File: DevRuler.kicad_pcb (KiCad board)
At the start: 2 copper layers, 205 x 30 mm, 2 parts

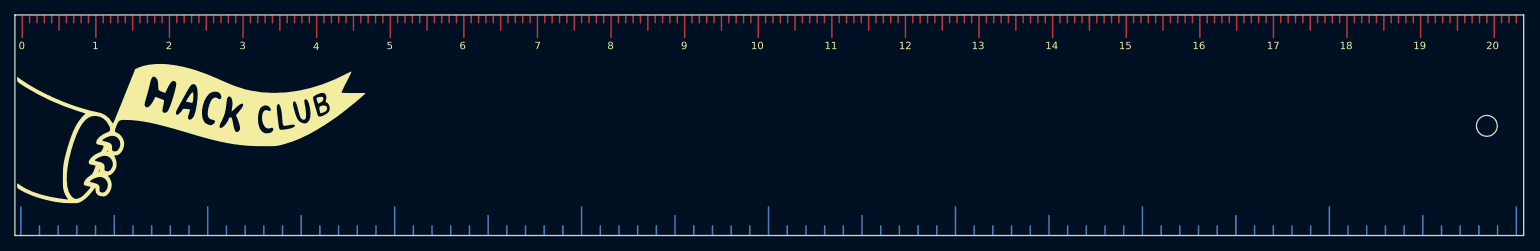
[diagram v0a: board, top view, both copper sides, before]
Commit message: Update LOGO footprint UUIDs, position and silkscreen
Modify DevRuler.kicad_pcb LOGO footprint: replace multiple UUIDs, change the footprint origin (from at 230 93 180 to at 152.5 97), and move/rewrap silkscreen polygons from B.SilkS to F.SilkS with updated fp_poly coordinates. These edits reposition and refresh the logo artwork on the front silkscreen and update element identifiers; no pad/net definitions were altered.
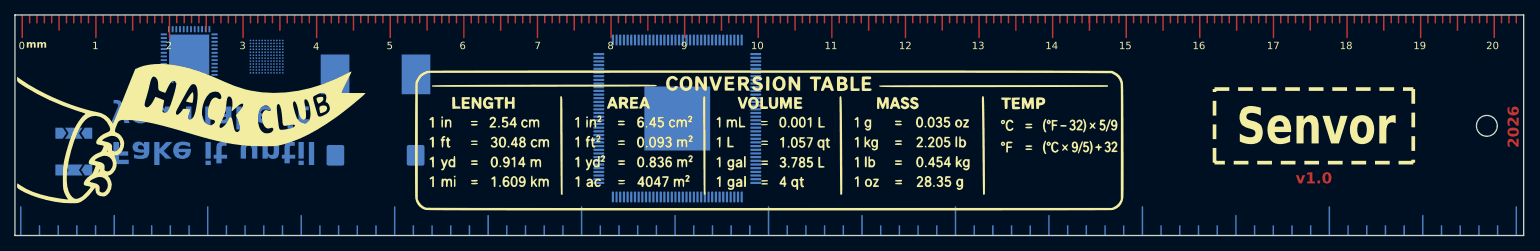
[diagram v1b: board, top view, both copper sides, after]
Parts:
- added G***: LOGO, LOGO, F.Cu at (152.5, 97.0)
- added G***: LOGO, LOGO, B.Cu at (187.0, 93.0)
- added REF**: ST_WLCSP-144_Die470, Package_CSP:ST_WLCSP-144_Die470, B.Cu at (84.2, 85.6)
- added REF**: EQFP-144-1EP_20x20mm_P0.5mm_EP8.93x8.7mm, Package_QFP:EQFP-144-1EP_20x20mm_P0.5mm_EP8.93x8.7mm, B.Cu at (140.0, 94.0)
- added REF**: OSHW-Symbol_13.4x12mm_SilkScreen, Symbol:OSHW-Symbol_13.4x12mm_SilkScreen, B.Cu at (58.0, 87.0)
- added REF**: SolderJumper-3_P2.0mm_Open_TrianglePad1.0x1.5mm, Jumper:SolderJumper-3_P2.0mm_Open_TrianglePad1.0x1.5mm, B.Cu at (58.0, 96.0)
- added REF**: L_Neosid_SM-NE127_HandSoldering, Inductor_SMD:L_Neosid_SM-NE127_HandSoldering, B.Cu at (99.0, 88.0)
- added REF**: Jumper_Harwin_S1621_P10.9mm, Jumper:Jumper_Harwin_S1621_P10.9mm, B.Cu at (99.0, 99.0)
- added REF**: Polarity_Center_Negative_6mm_SilkScreen, Symbol:Polarity_Center_Negative_6mm_SilkScreen, B.Cu at (117.0, 94.0)
- added REF**: QFN-48-1EP_7x7mm_P0.5mm_EP5.45x5.45mm, Package_DFN_QFN:QFN-48-1EP_7x7mm_P0.5mm_EP5.45x5.45mm, B.Cu at (73.7, 85.3)
- added REF**: SolderJumper-3_P2.0mm_Open_TrianglePad1.0x1.5mm, Jumper:SolderJumper-3_P2.0mm_Open_TrianglePad1.0x1.5mm, B.Cu at (58.0, 101.0)
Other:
- board text added: "2026"
- board text added: "DevRuler"
- board text added: "Fake it until you Make it"
- board text added: "Senvor"
- board text added: "in"
- board text added: "mm"
- board text added: "v1.0"

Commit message: Update PCB file: stackup, footprints and artwork
Add explicit board stackup and material parameters, enable copper/dielectric settings, and adjust CAM output (drillshape -> 0, outputdirectory -> DevRuler/). Reposition logo footprint and replace an existing WLCSP footprint with an OSHW symbol (new geometry, silkscreen polygon and updated properties/UUIDs). Add/update multiple footprints (solder jumper, inductor, and others), refine silkscreen/courtyard/fab primitives, pad shapes and attributes, and update many UUIDs. Also include updated DevRuler.kicad_pro and add DevRuler.zip (packaged artifacts) to prepare the project for fabrication and library cleanup.
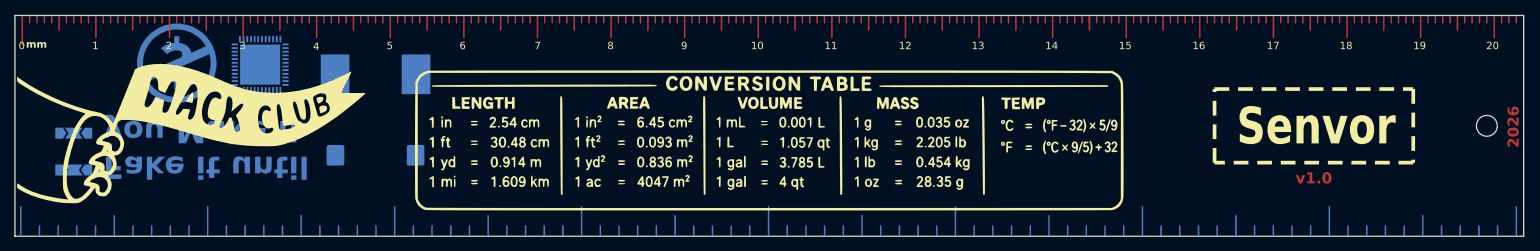
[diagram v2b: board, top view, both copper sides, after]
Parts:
- removed the REF** at (84.2, 85.6)
- removed the REF** at (140.0, 94.0)
- added REF**: Symbol_CC-Noncommercial_CopperTop_Big, Symbol:Symbol_CC-Noncommercial_CopperTop_Big, B.Cu at (72.0, 86.5)
- moved G*** 14.0 mm to (173.0, 93.0)
- moved REF** 9.74 mm to (83.3, 86.7)
- moved G*** 6.00 mm to (236.0, 93.0)
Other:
- outline, holes or cut-outs redrawn
